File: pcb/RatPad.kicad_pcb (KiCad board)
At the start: 2 copper layers, 113 x 55.5 mm, 26 parts, among them SW1 SW_Push, SW2 SW_Push, SW3 SW_Push, SW4 SW_Push, SW5 SW_Push, SW6 SW_Push, SW7 SW_Push, SW8 SW_Push, U1 XIAO-RP2040-DIP

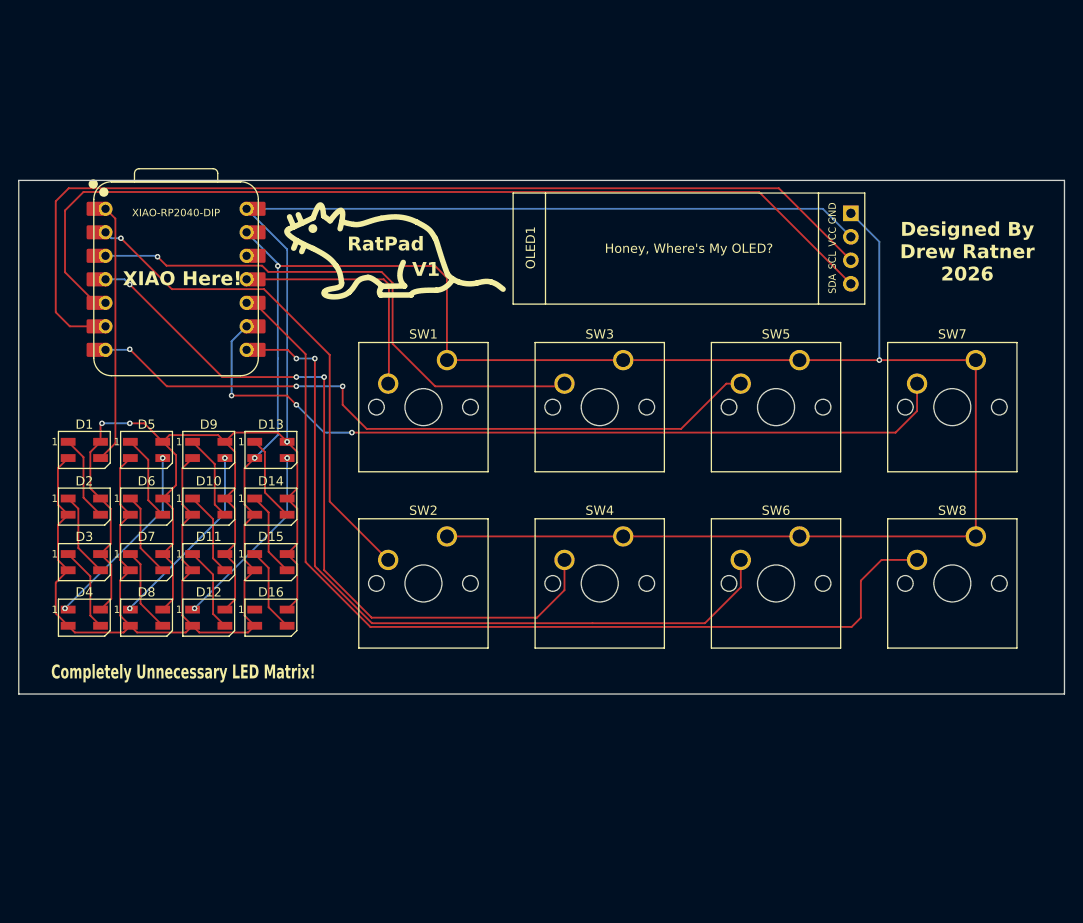
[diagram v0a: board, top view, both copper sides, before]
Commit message: Add case and update PCB
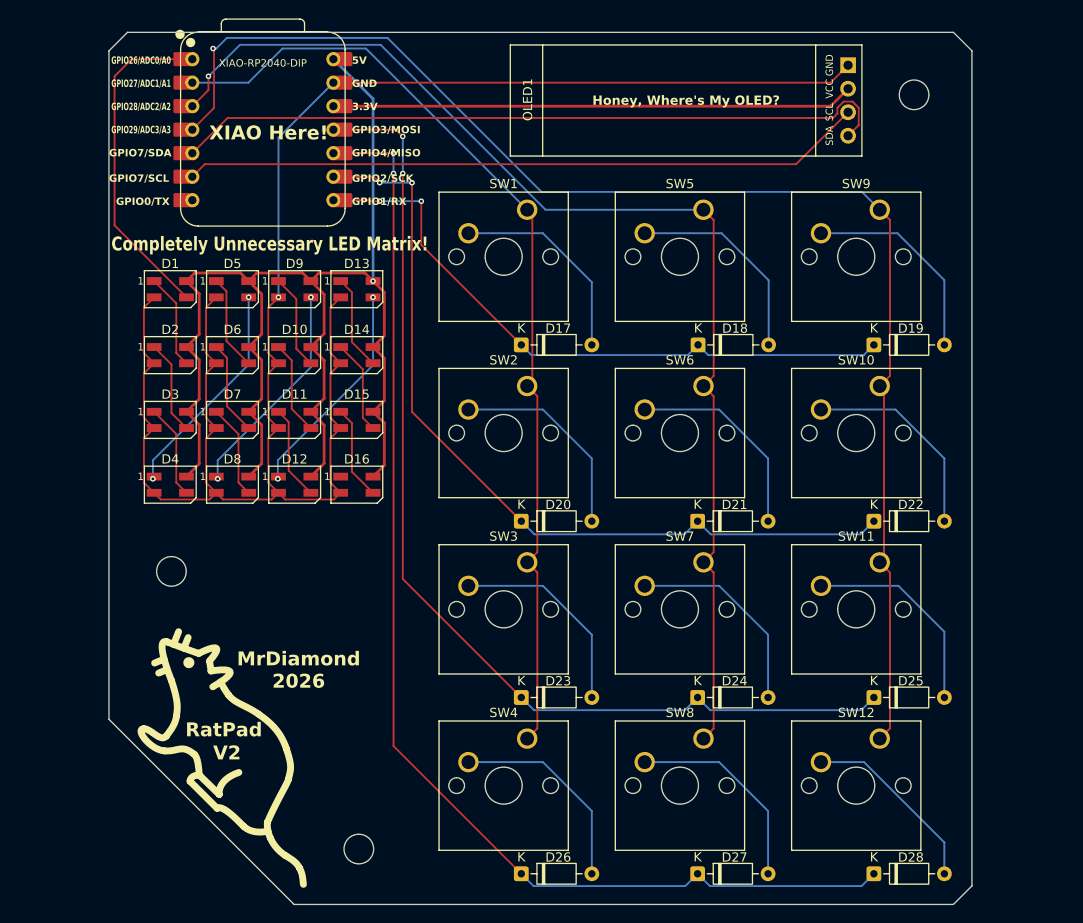
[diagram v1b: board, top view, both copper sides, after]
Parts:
- added D17: 1N4148, Diode_THT:D_DO-35_SOD27_P7.62mm_Horizontal, F.Cu at (146.3, 88.5)
- added D18: 1N4148, Diode_THT:D_DO-35_SOD27_P7.62mm_Horizontal, F.Cu at (165.4, 88.5)
- added D19: 1N4148, Diode_THT:D_DO-35_SOD27_P7.62mm_Horizontal, F.Cu at (184.4, 88.5)
- added D20: 1N4148, Diode_THT:D_DO-35_SOD27_P7.62mm_Horizontal, F.Cu at (146.3, 107.6)
- added D21: 1N4148, Diode_THT:D_DO-35_SOD27_P7.62mm_Horizontal, F.Cu at (165.4, 107.6)
- added D22: 1N4148, Diode_THT:D_DO-35_SOD27_P7.62mm_Horizontal, F.Cu at (184.4, 107.6)
- added D23: 1N4148, Diode_THT:D_DO-35_SOD27_P7.62mm_Horizontal, F.Cu at (146.3, 126.6)
- added D24: 1N4148, Diode_THT:D_DO-35_SOD27_P7.62mm_Horizontal, F.Cu at (165.4, 126.6)
- added D25: 1N4148, Diode_THT:D_DO-35_SOD27_P7.62mm_Horizontal, F.Cu at (184.4, 126.6)
- added D26: 1N4148, Diode_THT:D_DO-35_SOD27_P7.62mm_Horizontal, F.Cu at (146.3, 145.7)
- added D27: 1N4148, Diode_THT:D_DO-35_SOD27_P7.62mm_Horizontal, F.Cu at (165.4, 145.7)
- added D28: 1N4148, Diode_THT:D_DO-35_SOD27_P7.62mm_Horizontal, F.Cu at (184.4, 145.7)
- added REF**: MountingHole_3.2mm_M3, MountingHole:MountingHole_3.2mm_M3, F.Cu at (188.8, 61.5)
- added REF**: MountingHole_3.2mm_M3, MountingHole:MountingHole_3.2mm_M3, F.Cu at (108.5, 113.0)
- added REF**: MountingHole_3.2mm_M3, MountingHole:MountingHole_3.2mm_M3, F.Cu at (128.8, 143.0)
- added SW10: SW_Push, Button_Switch_Keyboard:SW_Cherry_MX_1.00u_PCB, F.Cu at (185.0, 93.0)
- added SW11: SW_Push, Button_Switch_Keyboard:SW_Cherry_MX_1.00u_PCB, F.Cu at (185.0, 112.0)
- added SW12: SW_Push, Button_Switch_Keyboard:SW_Cherry_MX_1.00u_PCB, F.Cu at (185.0, 131.1)
- added SW9: SW_Push, Button_Switch_Keyboard:SW_Cherry_MX_1.00u_PCB, F.Cu at (185.0, 73.9)
- moved SW7 36.7 mm to (166.0, 112.0)
- moved SW8 36.7 mm to (166.0, 131.1)
- moved SW3 24.2 mm to (146.9, 112.0)
- moved SW4 24.2 mm to (146.9, 131.1)
- moved D1 19.7 mm to (108.4, 82.5)
- moved D13 19.7 mm to (128.5, 82.5)
- moved D5 19.7 mm to (115.1, 82.5)
- moved D9 19.7 mm to (121.8, 82.5)
- moved SW5 19.3 mm to (166.0, 73.9)
- moved SW6 19.3 mm to (166.0, 93.0)
- moved D10 18.8 mm to (121.8, 89.6)
- moved D14 18.8 mm to (128.5, 89.6)
- moved D2 18.8 mm to (108.4, 89.6)
- moved D6 18.8 mm to (115.1, 89.6)
- moved U1 18.7 mm to (118.4, 65.3)
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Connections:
- OLED1 pad 2: +5V -> +3.3V
- SW1 pad 1: GND -> Col 1
- SW1 pad 2: Net-(U1-GPIO3/MOSI) -> Net-(D17-A)
- SW2 pad 1: GND -> Col 1
- SW2 pad 2: Net-(U1-GPIO27/ADC1/A1) -> Net-(D20-A)
- SW3 pad 1: GND -> Col 1
- SW3 pad 2: Net-(U1-GPIO28/ADC2/A2) -> Net-(D23-A)
- SW4 pad 1: GND -> Col 1
- SW4 pad 2: Net-(U1-GPIO29/ADC3/A3) -> Net-(D26-A)
- SW5 pad 1: GND -> Col 2
- SW5 pad 2: Net-(U1-GPIO0/TX) -> Net-(D18-A)
- SW6 pad 1: GND -> Col 2
- SW6 pad 2: Net-(U1-GPIO1/RX) -> Net-(D21-A)
- SW7 pad 1: GND -> Col 2
- SW7 pad 2: Net-(U1-GPIO2/SCK) -> Net-(D24-A)
- SW8 pad 1: GND -> Col 2
- SW8 pad 2: Net-(U1-GPIO4/MISO) -> Net-(D27-A)
- U1 pad 10: Net-(U1-GPIO4/MISO) -> Row 4
- U1 pad 11: Net-(U1-GPIO3/MOSI) -> Row 3
- U1 pad 12: unconnected-(U1-3V3-Pad12) -> +3.3V
- U1 pad 2: Net-(U1-GPIO27/ADC1/A1) -> Col 1
- U1 pad 3: Net-(U1-GPIO28/ADC2/A2) -> Col 2
- U1 pad 4: Net-(U1-GPIO29/ADC3/A3) -> Col 3
- U1 pad 7: Net-(U1-GPIO0/TX) -> unconnected-(U1-GPIO0/TX-Pad7)
- U1 pad 8: Net-(U1-GPIO1/RX) -> Row 1
- U1 pad 9: Net-(U1-GPIO2/SCK) -> Row 2
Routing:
- net Col 3: track 0.00 -> 149.3 mm, vias 0 -> 1
- net Row 4: track 0.00 -> 130.4 mm, vias 0 -> 2
- net Col 2: track 0.00 -> 126.1 mm, vias 0 -> 1
- net Row 3: track 0.00 -> 114.1 mm, vias 0 -> 2
- net GND: track 311.0 -> 199.5 mm, vias 3 -> 1
- net Net-(U1-GPIO4/MISO): track 104.6 -> 0.00 mm
- net Col 1: track 0.00 -> 104.4 mm
- net Row 2: track 0.00 -> 90.7 mm, vias 0 -> 2
- net Net-(U1-GPIO2/SCK): track 87.8 -> 0.00 mm, vias 3 -> 0
- net Net-(U1-GPIO1/RX): track 83.3 -> 0.00 mm, vias 2 -> 0
- net Net-(U1-GPIO29/ADC3/A3): track 81.5 -> 0.00 mm, vias 3 -> 0
- net Net-(U1-GPIO0/TX): track 75.4 -> 0.00 mm, vias 3 -> 0
- net Row 1: track 0.00 -> 69.5 mm, vias 0 -> 2
- net Net-(U1-GPIO28/ADC2/A2): track 59.7 -> 0.00 mm, vias 1 -> 0
- net +5V: track 202.7 -> 146.1 mm, vias 3 -> 1
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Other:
- board size 113 x 55.5 mm -> 93.2 x 94.2 mm
- board text added: "3.3V"
- board text added: "5V"
- board text added: "GND"
- board text added: "GPIO0/TX"
- board text added: "GPIO1/RX"
- board text added: "GPIO2/SCK"
- board text added: "GPIO26/ADC0/A0"
- board text added: "GPIO27/ADC1/A1"
- board text added: "GPIO28/ADC2/A2"
- board text added: "GPIO29/ADC3/A3"
- board text added: "GPIO3/MOSI"
- board text added: "GPIO4/MISO"
- board text added: "GPIO7/SCL"
- board text added: "GPIO7/SDA"
- board text added: "MrDiamond 2026"
- board text added: "V2"
- board text removed: "Designed By Drew Ratner 2026"
- board text removed: "V1"
